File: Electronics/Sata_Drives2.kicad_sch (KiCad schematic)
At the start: 66 parts, among them J22 47018-2000, J23 47018-2000, Q10 NPN, Q11 PMOS, Q12 NPN, Q13 PMOS, Q14 PMOS, Q15 NPN, Q16 NPN, Q17 PMOS, U11 W25X40CLSN, U12 JMS561, Y2 30MHz

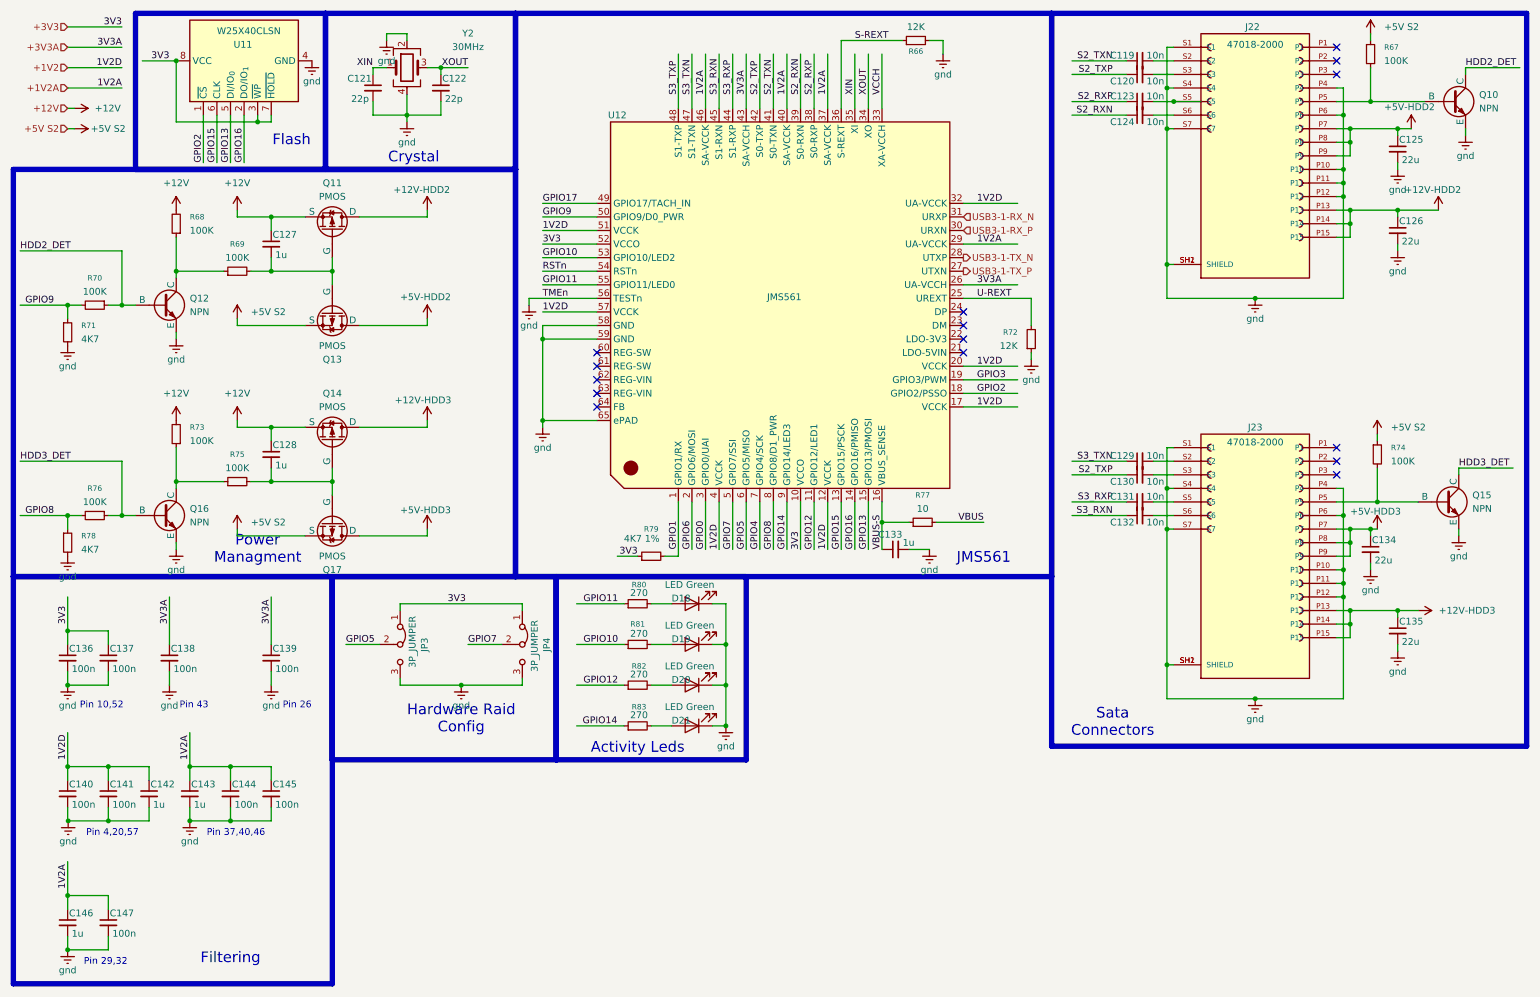
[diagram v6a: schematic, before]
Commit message: Changed sata port
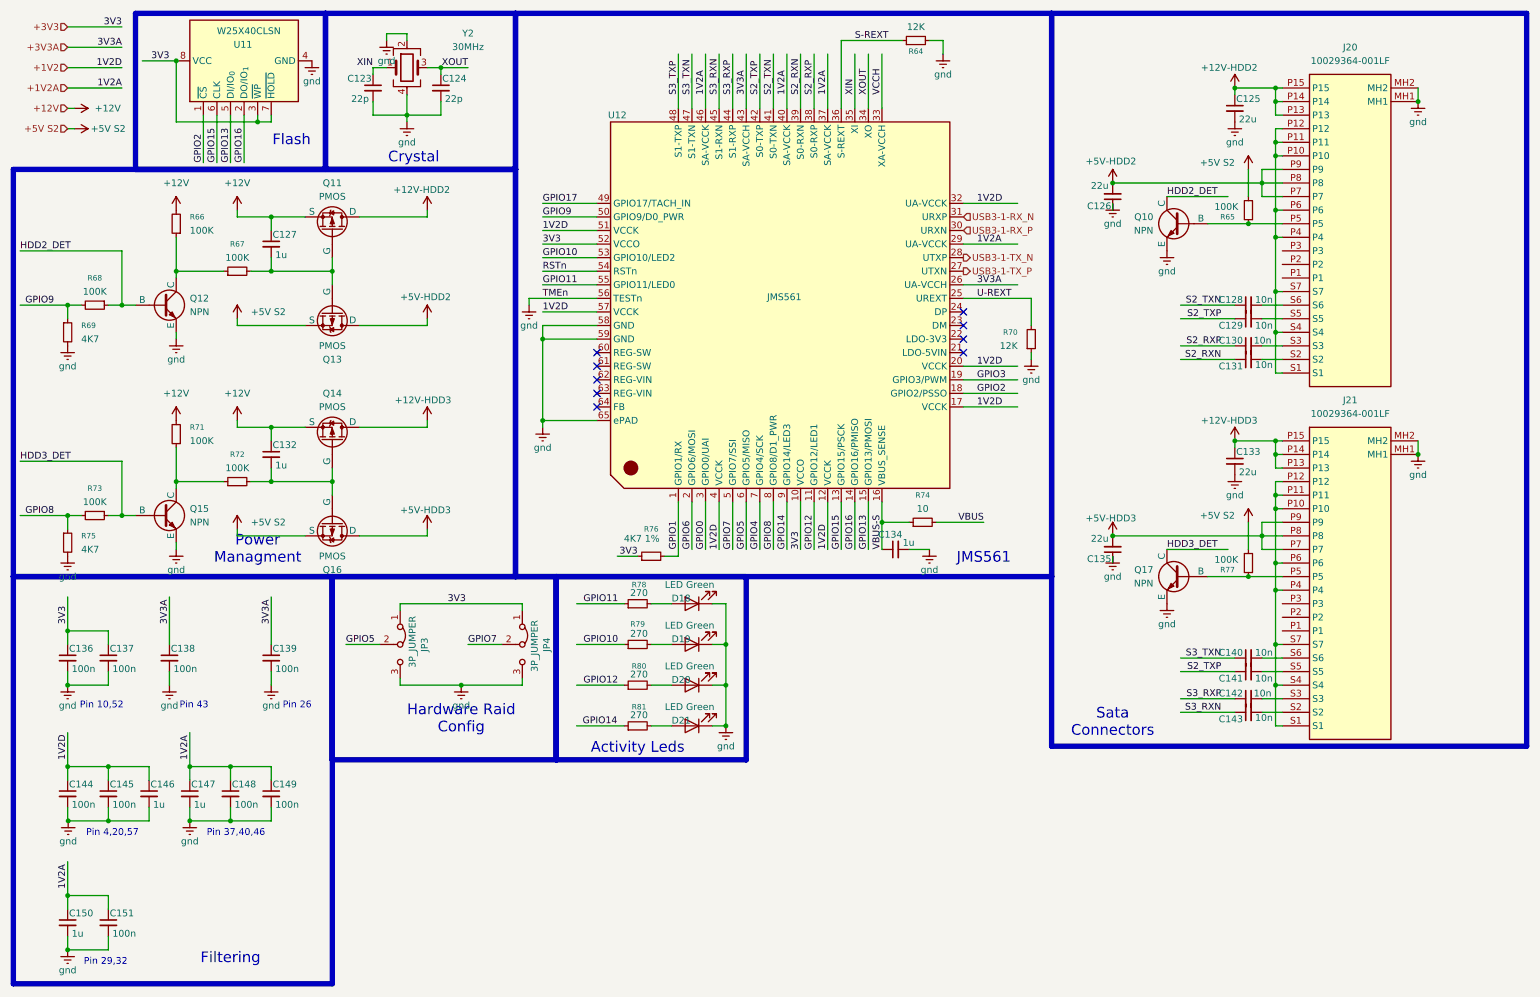
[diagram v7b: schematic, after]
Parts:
- removed C119, C120, C123, C124, C132: 10n, Capacitor_SMD:C_0402_1005Metric, symbol Device:C_Small
- removed C134: 22u, Capacitor_SMD:C_1206_3216Metric, symbol Device:C_Small
- removed J22, J23: 47018-2000, 47018-2000:MOLEX_47018-2000, symbol 47018-2000:47018-2000
- removed Q15: NPN, MMBT3904:P200_SOT-23, symbol Simulation_SPICE:NPN
- removed R67, R74: 100K, Resistor_SMD:R_0603_1608Metric, symbol Device:R_Small
- added C128, C140, C141, C142, C143: 10n, Capacitor_SMD:C_0402_1005Metric, symbol Device:C_Small
- added C133: 22u, Capacitor_SMD:C_1206_3216Metric, symbol Device:C_Small
- added J20, J21: 10029364-001LF, 87713-1001:87713-1001, symbol 10029364-001LF:10029364-001LF
- added Q17: NPN, MMBT3904:P200_SOT-23, symbol Simulation_SPICE:NPN
- added R65, R77: 100K, Resistor_SMD:R_0603_1608Metric, symbol Device:R_Small
- U12: footprint Package_DFN_QFN:QFN-64-1EP_8x8mm_P0.4mm_EP6.5x6.5mm -> Package_DFN_QFN:QFN-64-1EP_8x8mm_P0.4mm_EP6.5x6.5mm_ThermalVias
- renumbered C121 to C123, C122 to C124, C128 to C132, C133 to C134, C140 to C144, C141 to C145, C142 to C146, C143 to C147, C144 to C148, C145 to C149, C146 to C150, C147 to C151, Q16 to Q15, Q17 to Q16, R66 to R64, R68 to R66, R69 to R67, R70 to R68, R71 to R69, R72 to R70, R73 to R71, R75 to R72, R76 to R73, R77 to R74, R78 to R75, R79 to R76, R80 to R78, R81 to R79, R82 to R80, R83 to R81
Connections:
- net +12V-HDD2: now also C125.1, J20.P13, J20.P14, J20.P15; no longer C126.1
- net +12V-HDD3: now also C133.1, J21.P13, J21.P14, J21.P15; no longer C135.1
- net +5V S2: now also R65.2, R77.2
- net +5V-HDD2: now also C126.2, J20.P7, J20.P8, J20.P9; no longer C125.1
- net +5V-HDD3: now also C135.2, J21.P7, J21.P8, J21.P9
- net HDD3_DET: now also Q17.1 (C)
- net S2_RXN: now also C131.1
- net S2_RXP: now also C130.1
- net S2_TXN: now also C128.1
- net S2_TXP: now also C129.1, C141.1; no longer C130.1
- net S3_RXN: now also C143.1
- net S3_RXP: now also C142.1; no longer C131.1
- net S3_TXN: now also C140.1; no longer C129.1
- net gnd: now also C126.1, C135.1, C133.2, J20.MH1, J20.MH2, J21.MH1, J21.MH2, Q17.3 (E); no longer C126.2, C135.2
- net at Q10.2 (B): now also J20.P5, R65.1
- net at C129.2: now also J20.S5
- net at C130.2: now also J20.S3
- net at C131.2: now also J20.S2
- new net: C141.2, J21.S5
- new net: J21.P10, J21.P11, J21.P12, J21.P4, J21.P6, J21.S1, J21.S4, J21.S7
- new net: J21.P5, Q17.2 (B), R77.1
- new net: C143.2, J21.S2
- new net: C142.2, J21.S3
- new net: C140.2, J21.S6
- new net: J20.P10, J20.P11, J20.P12, J20.P4, J20.P6, J20.S1, J20.S4, J20.S7
- new net: C128.2, J20.S6
- no-connect marks 15 -> 9

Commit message: More pcbing
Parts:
- removed J20, J21: 10029364-001LF, 87713-1001:87713-1001, symbol 10029364-001LF:10029364-001LF
- added J20, J21: 0877131001, 87713-1001:87713-1001, symbol 0877131001:0877131001
- renumbered C123 to C124, C124 to C125, C125 to C126, C126 to C127, C127 to C128, C128 to C129, C129 to C130, C130 to C131, C131 to C132, C132 to C133, C133 to C134, C134 to C135, C135 to C136, C136 to C137, C137 to C138, C138 to C139, C139 to C140, C140 to C141, C141 to C142, C142 to C143, C143 to C144, C144 to C145, C145 to C146, C146 to C147, C147 to C148, C148 to C149, C149 to C150, C150 to C151, C151 to C152
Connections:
- net +12V-HDD2: now also J20.20 (P13), J20.21 (P14), J20.22 (P15)
- net +12V-HDD3: now also J21.20 (P13), J21.21 (P14), J21.22 (P15)
- net +5V-HDD2: now also J20.14 (P7), J20.15 (P8), J20.16 (P9)
- net +5V-HDD3: now also J21.14 (P7), J21.15 (P8), J21.16 (P9)
- net gnd: now also J20.1 (S1), J20.11 (P4), J20.13 (P6), J20.17 (P10), J20.18 (P11), J20.19 (P12), J20.4 (S4), J20.7 (S7), J21.1 (S1), J21.11 (P4), J21.13 (P6), J21.17 (P10), J21.18 (P11), J21.19 (P12), J21.4 (S4), J21.7 (S7)
- net at C142.2: now also J21.5 (S5)
- net at Q10.2 (B), R65.1: now also J20.12 (P5)
- net at C132.2: now also J20.2 (S2)
- net at Q17.2 (B), R77.1: now also J21.12 (P5)
- net at C144.2: now also J21.2 (S2)
- net at C143.2: now also J21.3 (S3)
- net at C141.2: now also J21.6 (S6)
- net at C130.2: now also J20.5 (S5)
- net at C131.2: now also J20.3 (S3)
- net at C129.2: now also J20.6 (S6)
- no-connect marks 9 -> 15
